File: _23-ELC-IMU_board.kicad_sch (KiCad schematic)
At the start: 9 parts, among them J1 Deutsch DT6, J2 Deutsch DT6, J3 Conn_01x03

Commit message: Redo of placement
Really like this attempt
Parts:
- J1, J2: value Deutsch DT6 -> MX150; footprint Global Libraries:TE_DT15-6P -> Connector_Molex:Molex_Micro-Fit_3.0_43045-0600_2x03_P3.00mm_Horizontal
- J3: footprint Connector_PinHeader_1.27mm:PinHeader_1x03_P1.27mm_Vertical_SMD_Pin1Left -> Connector_PinHeader_1.27mm:PinHeader_1x03_P1.27mm_Vertical
- R1: footprint Resistor_SMD:R_0201_0603Metric -> Resistor_SMD:R_0603_1608Metric_Pad0.98x0.95mm_HandSolder
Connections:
- net CANH renamed CAN+
- net CANL renamed CAN-

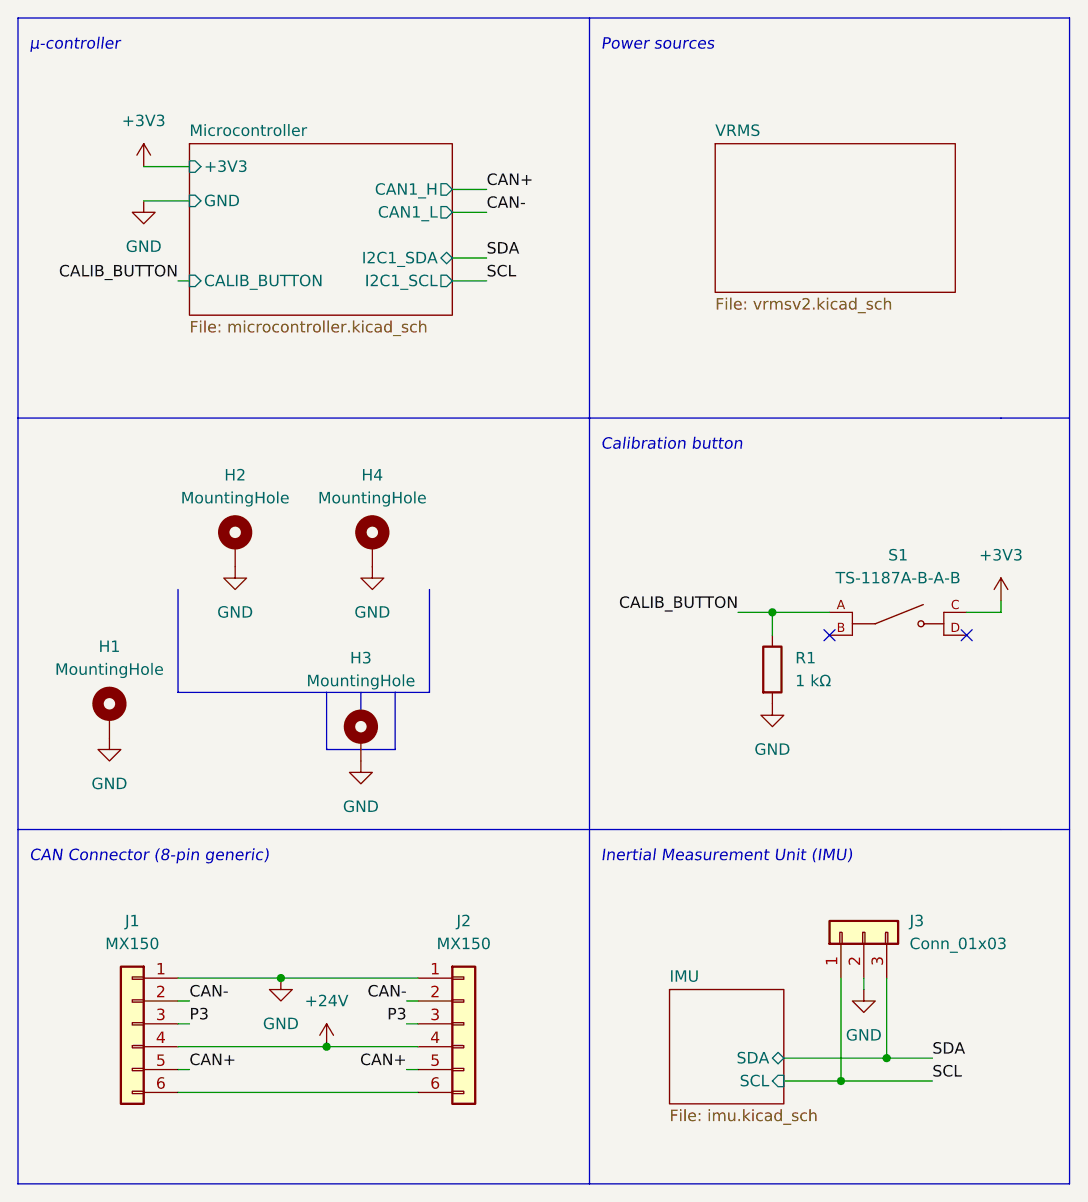
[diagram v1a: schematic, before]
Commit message: Added 0 Ohm resistor between shield (grounded)
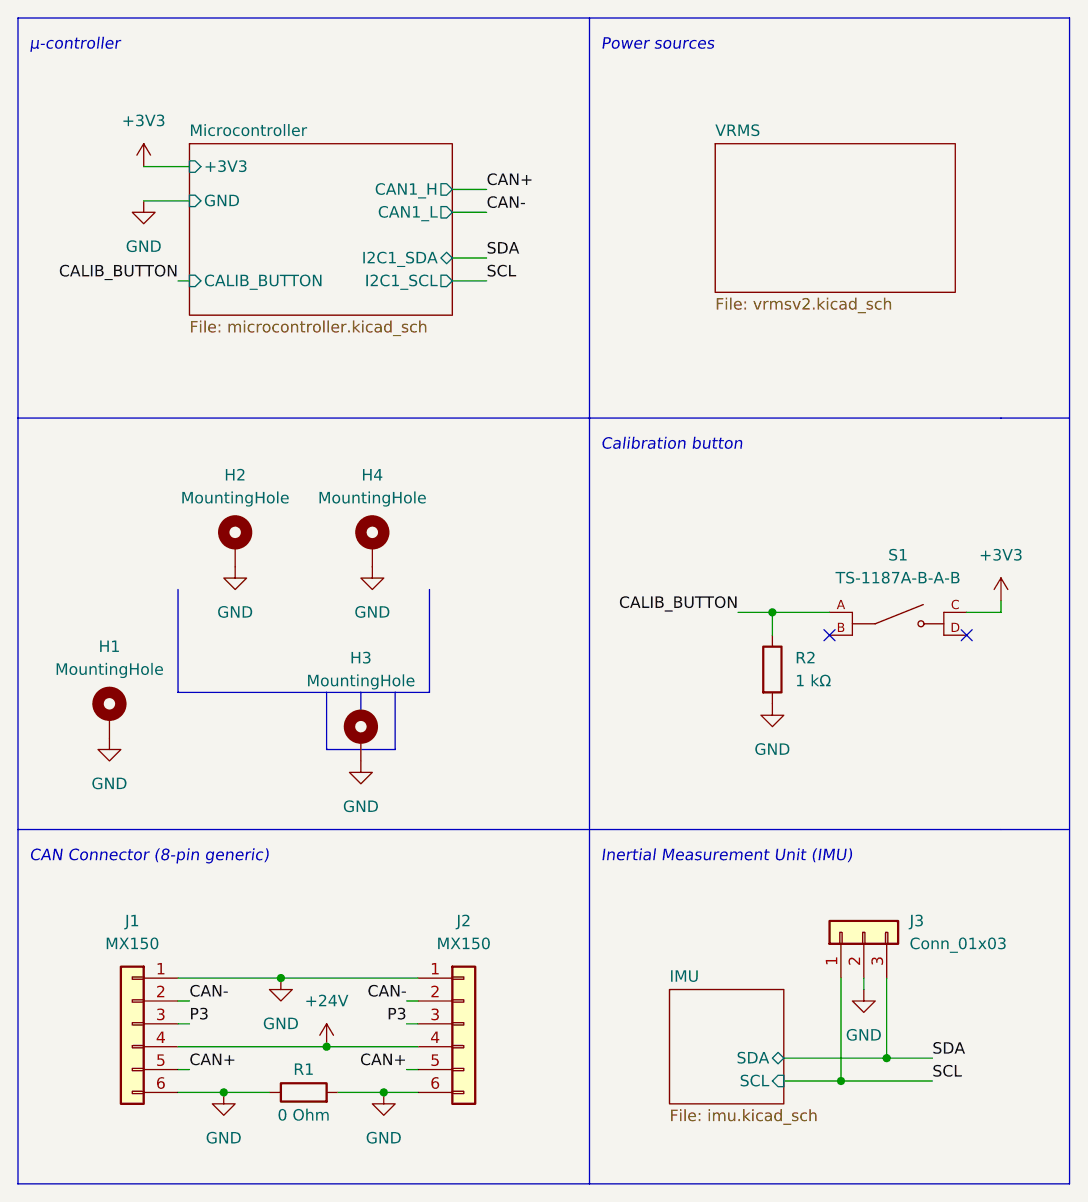
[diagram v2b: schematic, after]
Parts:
- added R1: 0 Ohm, Resistor_SMD:R_0603_1608Metric_Pad0.98x0.95mm_HandSolder, symbol Device:R
- renumbered R1 to R2
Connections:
- net GND: now also J1.6 (Pin_6), J2.6 (Pin_6), R1.1, R1.2
